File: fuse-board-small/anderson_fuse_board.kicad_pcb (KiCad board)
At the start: 2 copper layers, 48.5 x 105 mm, 13 parts, among them J1 Anderson_two_redblack, J2 Anderson_two_redblack, J3 Anderson_two_redblack, J4 Anderson_two_redblack, J5 Anderson_two_redblack

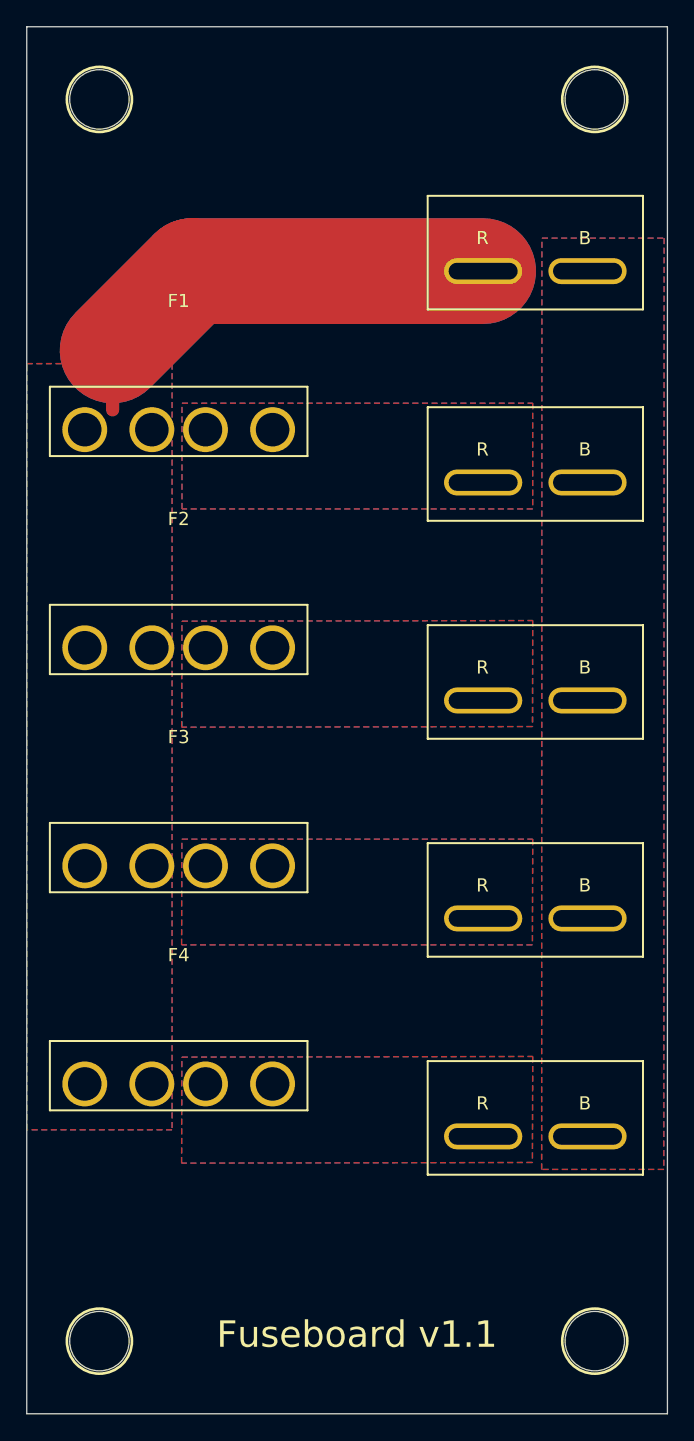
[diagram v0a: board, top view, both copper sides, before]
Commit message: fuse-board-small v1.1:
- Update straight Anderson footprint for fixed silk, bigger copper ring
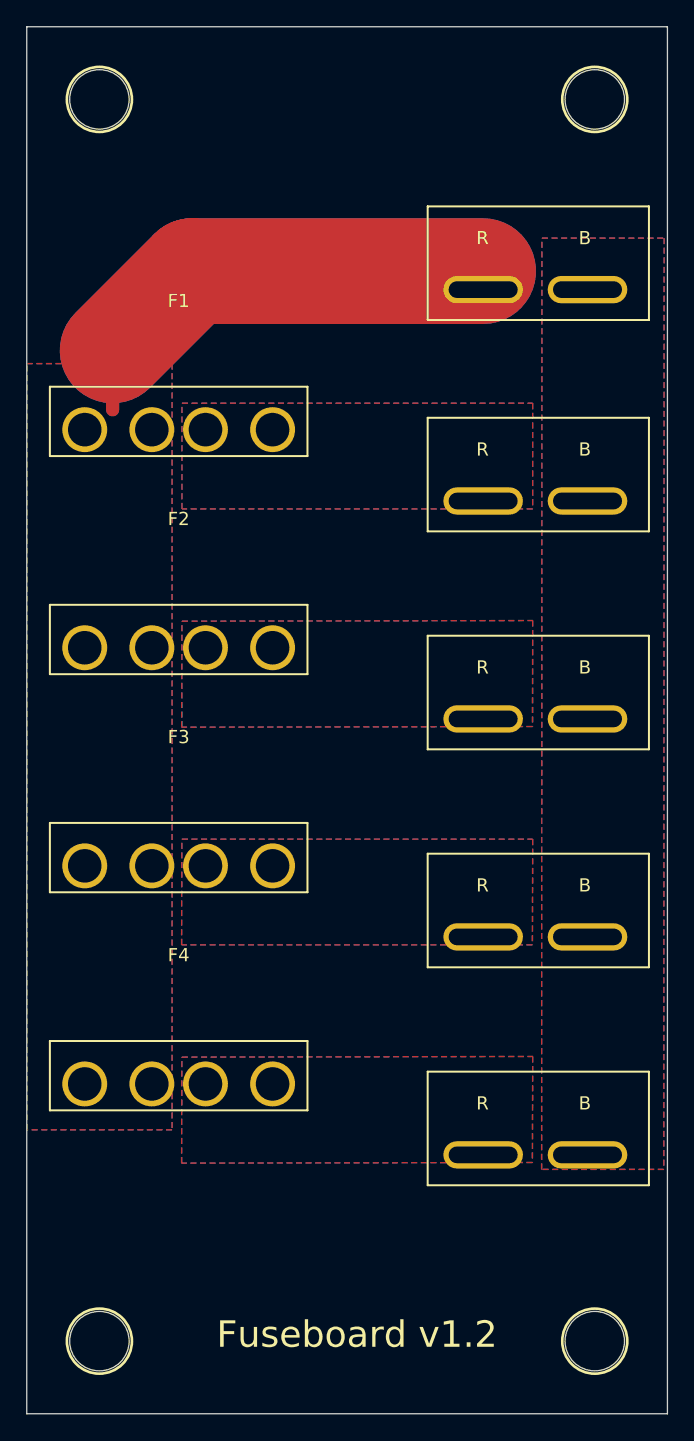
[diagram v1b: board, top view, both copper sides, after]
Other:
- board text added: "Fuseboard v1.2"
- board text removed: "Fuseboard v1.1"
